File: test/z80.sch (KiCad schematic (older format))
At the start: 48 parts, among them U1 74AHC1G14

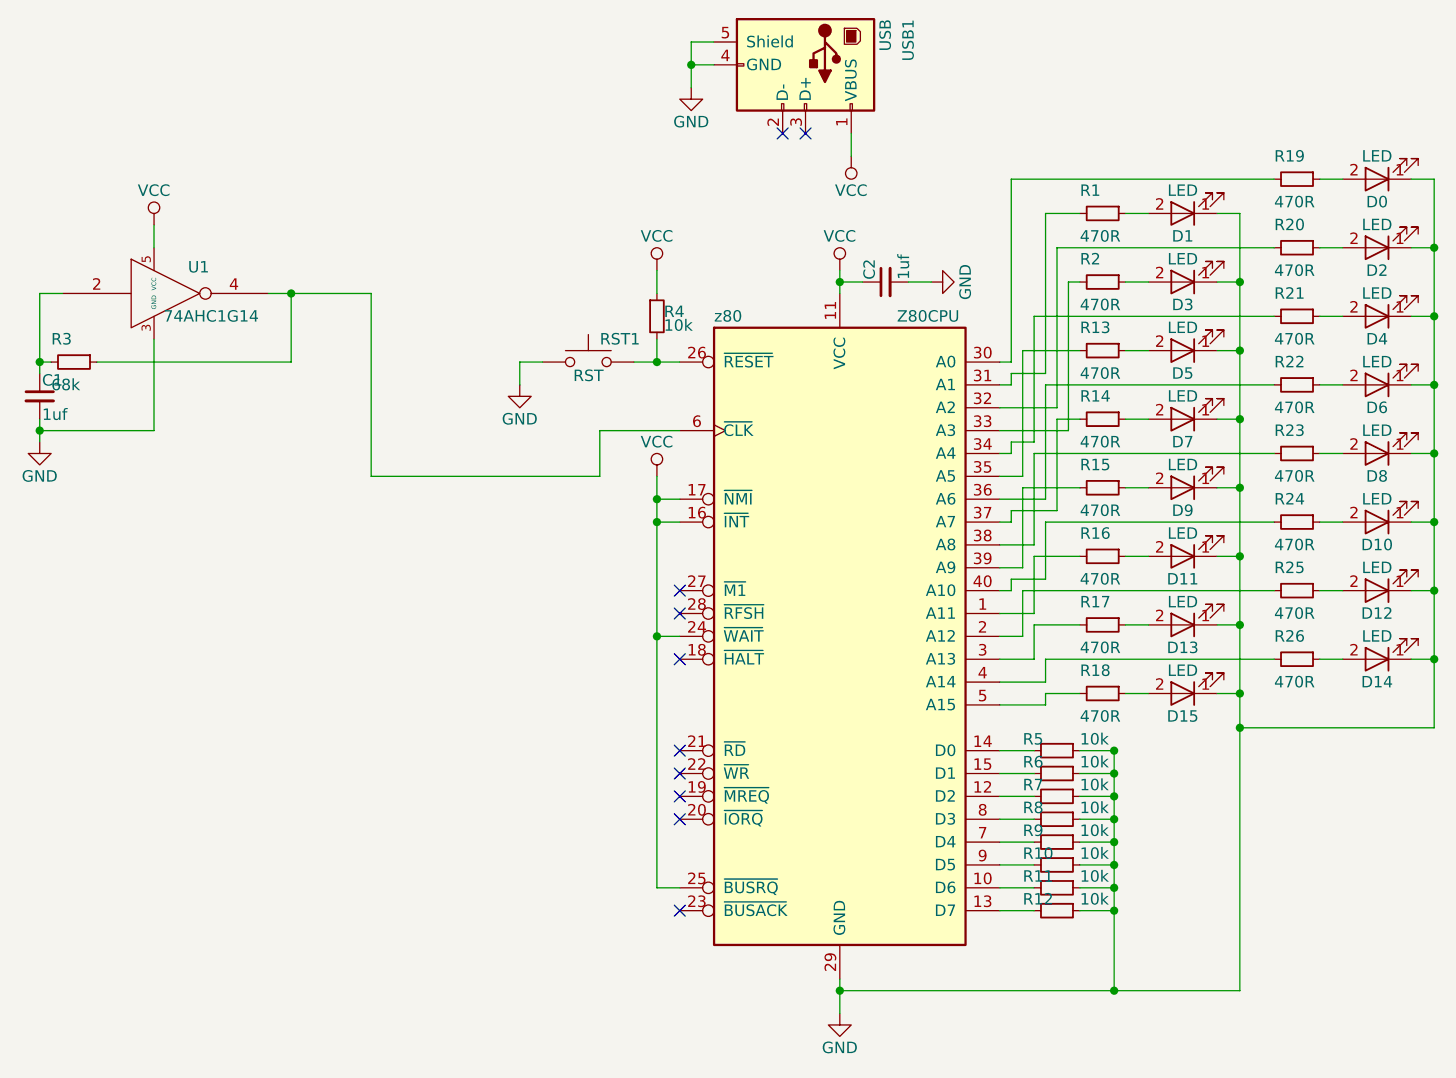
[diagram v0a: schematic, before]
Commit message: Added jumper on clock signal and replaced C1 with THT footprint.
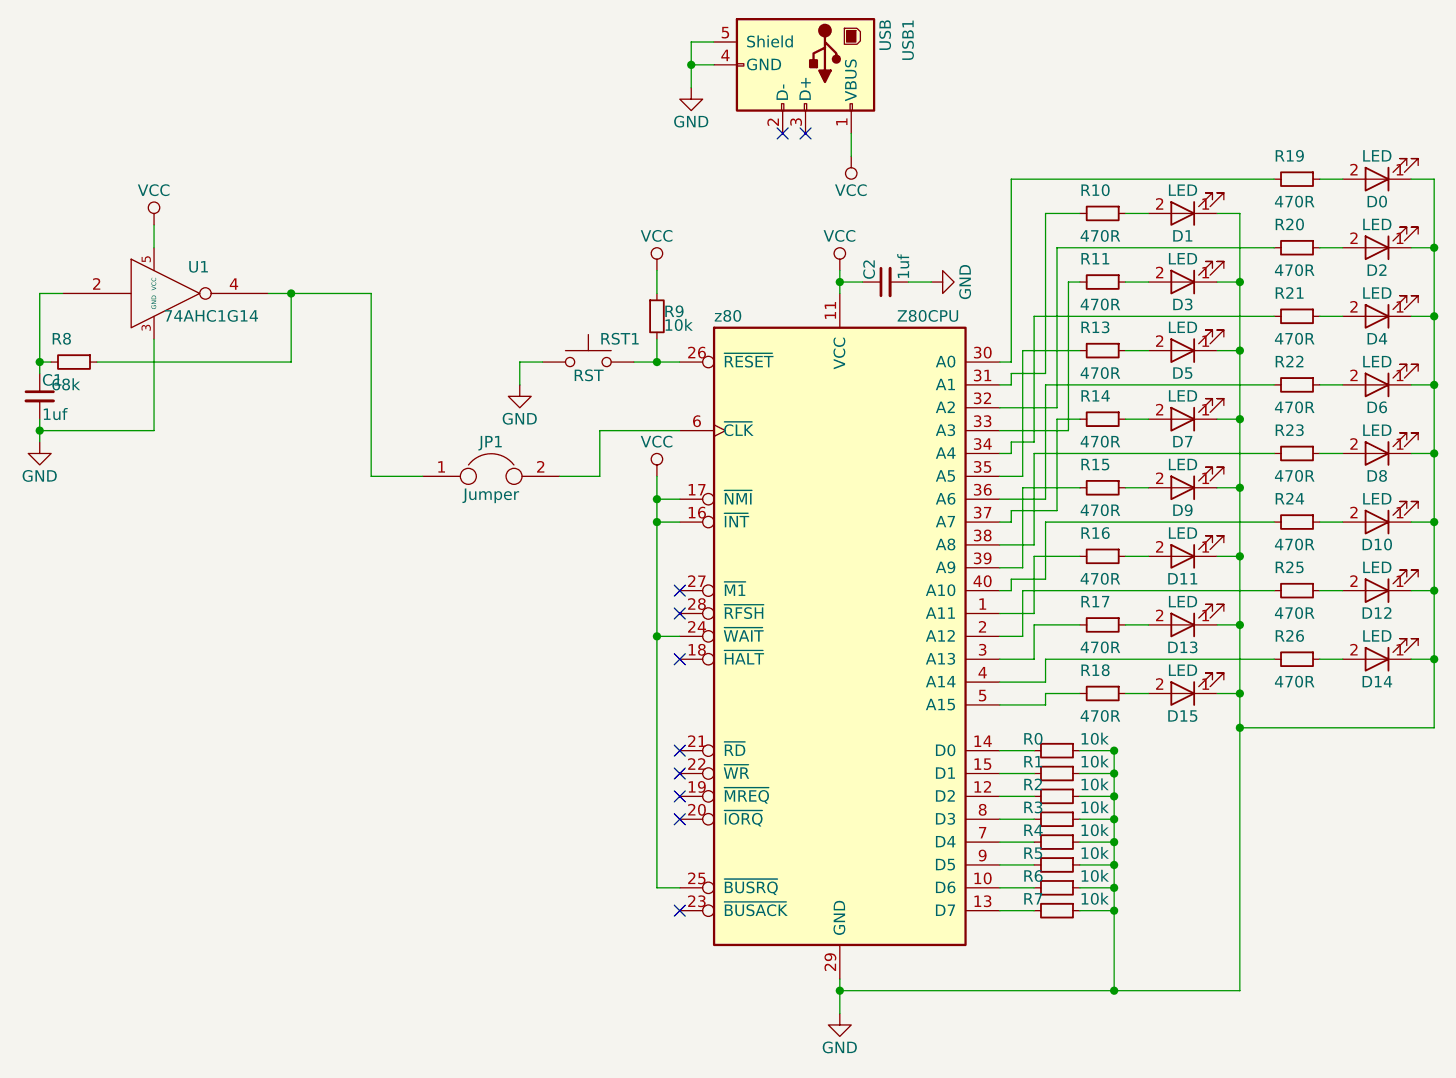
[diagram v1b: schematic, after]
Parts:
- added JP1: Jumper, Pin_Headers:Pin_Header_Straight_1x02_Pitch2.54mm, symbol Jumper
- C1: footprint Capacitors_SMD:C_0805_HandSoldering -> Capacitors_THT:CP_Radial_D4.0mm_P2.00mm
- renumbered R5 to R0, R6 to R1, R1 to R10, R2 to R11, R7 to R2, R8 to R3, R9 to R4, R10 to R5, R11 to R6, R12 to R7, R3 to R8, R4 to R9
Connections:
- net at R8.1, U1.4: now also JP1.1; no longer z80.6 (~CLK~)
- new net: JP1.2, z80.6 (~CLK~)
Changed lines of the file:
@@
 $EndComp
 $Comp
-L R_Small R5
+L R_Small R0
 U 1 1 59450825
 P 6300 4750
-F 0 "R5" V 6250 4600 50  0000 L CNN
+F 0 "R0" V 6250 4600 50  0000 L CNN
 F 1 "10k" V 6250 4850 50  0000 L CNN
 F 2 "Resistors_SMD:R_0805_HandSoldering" H 6300 4750 50  0001 C CNN
@@
 $EndComp
 $Comp
-L R_Small R6
+L R_Small R1
 U 1 1 5945082B
 P 6300 4850
-F 0 "R6" V 6250 4700 50  0000 L CNN
+F 0 "R1" V 6250 4700 50  0000 L CNN
 F 1 "10k" V 6250 4950 50  0000 L CNN
 F 2 "Resistors_SMD:R_0805_HandSoldering" H 6300 4850 50  0001 C CNN
@@
 $EndComp
 $Comp
-L R_Small R7
+L R_Small R2
 U 1 1 59450831
 P 6300 4950
-F 0 "R7" V 6250 4800 50  0000 L CNN
+F 0 "R2" V 6250 4800 50  0000 L CNN
 F 1 "10k" V 6250 5050 50  0000 L CNN
 F 2 "Resistors_SMD:R_0805_HandSoldering" H 6300 4950 50  0001 C CNN
@@
 $EndComp
 $Comp
-L R_Small R8
+L R_Small R3
 U 1 1 59450837
 P 6300 5050
-F 0 "R8" V 6250 4900 50  0000 L CNN
+F 0 "R3" V 6250 4900 50  0000 L CNN
 F 1 "10k" V 6250 5150 50  0000 L CNN
 F 2 "Resistors_SMD:R_0805_HandSoldering" H 6300 5050 50  0001 C CNN
@@
 $EndComp
 $Comp
-L R_Small R9
+L R_Small R4
 U 1 1 5945083D
 P 6300 5150
-F 0 "R9" V 6250 5000 50  0000 L CNN
+F 0 "R4" V 6250 5000 50  0000 L CNN
 F 1 "10k" V 6250 5250 50  0000 L CNN
 F 2 "Resistors_SMD:R_0805_HandSoldering" H 6300 5150 50  0001 C CNN
@@
 $EndComp
 $Comp
-L R_Small R10
+L R_Small R5
 U 1 1 59450843
 P 6300 5250
-F 0 "R10" V 6250 5100 50  0000 L CNN
+F 0 "R5" V 6250 5100 50  0000 L CNN
 F 1 "10k" V 6250 5350 50  0000 L CNN
 F 2 "Resistors_SMD:R_0805_HandSoldering" H 6300 5250 50  0001 C CNN
@@
 $EndComp
 $Comp
-L R_Small R11
+L R_Small R6
 U 1 1 59450849
 P 6300 5350
-F 0 "R11" V 6250 5200 50  0000 L CNN
+F 0 "R6" V 6250 5200 50  0000 L CNN
 F 1 "10k" V 6250 5450 50  0000 L CNN
 F 2 "Resistors_SMD:R_0805_HandSoldering" H 6300 5350 50  0001 C CNN
@@
 $EndComp
 $Comp
-L R_Small R12
+L R_Small R7
 U 1 1 5945084F
 P 6300 5450
-F 0 "R12" V 6250 5300 50  0000 L CNN
+F 0 "R7" V 6250 5300 50  0000 L CNN
 F 1 "10k" V 6250 5550 50  0000 L CNN
 F 2 "Resistors_SMD:R_0805_HandSoldering" H 6300 5450 50  0001 C CNN
@@
 NoConn ~ 4650 4150
 $Comp
-L R_Small R4
+L R_Small R9
 U 1 1 59458696
 P 4550 2850
-F 0 "R4" H 4580 2870 50  0000 L CNN
+F 0 "R9" H 4580 2870 50  0000 L CNN
 F 1 "10k" H 4580 2810 50  0000 L CNN
 F 2 "Resistors_SMD:R_0805_HandSoldering" H 4550 2850 50  0001 C CNN
@@
 F 0 "C1" H 1860 3270 50  0000 L CNN
 F 1 "1uf" H 1860 3120 50  0000 L CNN
-F 2 "Capacitors_SMD:C_0805_HandSoldering" H 1850 3200 50  0001 C CNN
+F 2 "Capacitors_THT:CP_Radial_D4.0mm_P2.00mm" H 1850 3200 50  0001 C CNN
 F 3 "" H 1850 3200 50  0001 C CNN
 	1    1850 3200
@@
 $EndComp
 $Comp
-L R_Small R3
+L R_Small R8
 U 1 1 59459C0E
 P 2000 3050
-F 0 "R3" V 1900 2950 50  0000 L CNN
+F 0 "R8" V 1900 2950 50  0000 L CNN
 F 1 "68k" V 2100 2950 50  0000 L CNN
 F 2 "Resistors_SMD:R_0805_HandSoldering" H 2000 3050 50  0001 C CNN
@@
 Connection ~ 2950 2750
 Wire Wire Line
-	3300 3550 4300 3550
-Wire Wire Line
 	3300 2750 3300 3550
 Wire Wire Line
@@
 	5350 5750 5350 5900
 Wire Wire Line
-	4300 3550 4300 3350
+	4300 3350 4300 3550
 Wire Wire Line
 	6400 5450 6550 5450
@@
 	6700 3900 6600 3900
 $Comp
-L R_Small R1
+L R_Small R10
 U 1 1 5954462D
 P 6500 2400
-F 0 "R1" V 6400 2300 50  0000 L CNN
+F 0 "R10" V 6400 2300 50  0000 L CNN
 F 1 "470R" V 6600 2300 50  0000 L CNN
 F 2 "Resistors_SMD:R_0805_HandSoldering" H 6500 2400 50  0001 C CNN
@@
 $EndComp
 $Comp
-L R_Small R2
+L R_Small R11
 U 1 1 59544633
 P 6500 2700
-F 0 "R2" V 6400 2600 50  0000 L CNN
+F 0 "R11" V 6400 2600 50  0000 L CNN
 F 1 "470R" V 6600 2600 50  0000 L CNN
 F 2 "Resistors_SMD:R_0805_HandSoldering" H 6500 2700 50  0001 C CNN
@@
 Wire Wire Line
 	2100 3050 2950 3050
+$Comp
+L Jumper JP1
+U 1 1 59597416
+P 3825 3550
+F 0 "JP1" H 3825 3700 50  0000 C CNN
+F 1 "Jumper" H 3825 3470 50  0000 C CNN
+F 2 "Pin_Headers:Pin_Header_Straight_1x02_Pitch2.54mm" H 3825 3550 50  0001 C CNN
+F 3 "" H 3825 3550 50  0001 C CNN
+	1    3825 3550
+	1    0    0    -1
+$EndComp
+Wire Wire Line
+	3300 3550 3525 3550
+Wire Wire Line
+	4300 3550 4125 3550
 $EndSCHEMATC

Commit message: Minor layout changes
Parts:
- C1: footprint Capacitors_THT:CP_Radial_D4.0mm_P2.00mm -> Capacitors_THT:C_Disc_D5.1mm_W3.2mm_P5.00mm
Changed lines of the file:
@@
 LIBS:Zilog
 LIBS:z80-cache
-EELAYER 25 0
+EELAYER 26 0
 EELAYER END
 $Descr A4 11693 8268
@@
 F 0 "C1" H 1860 3270 50  0000 L CNN
 F 1 "1uf" H 1860 3120 50  0000 L CNN
-F 2 "Capacitors_THT:CP_Radial_D4.0mm_P2.00mm" H 1850 3200 50  0001 C CNN
+F 2 "Capacitors_THT:C_Disc_D5.1mm_W3.2mm_P5.00mm" H 1850 3200 50  0001 C CNN
 F 3 "" H 1850 3200 50  0001 C CNN
 	1    1850 3200
